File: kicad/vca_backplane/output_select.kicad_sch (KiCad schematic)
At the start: 54 parts, among them J12 AudioJack_729JH, J8 AudioJack_729JH, U1 DG442xY, U12 DG442xY, U13 NE5532, U3 MCP4822, U5 AS3360, U8 PCA9555PW, U9 DG442xY

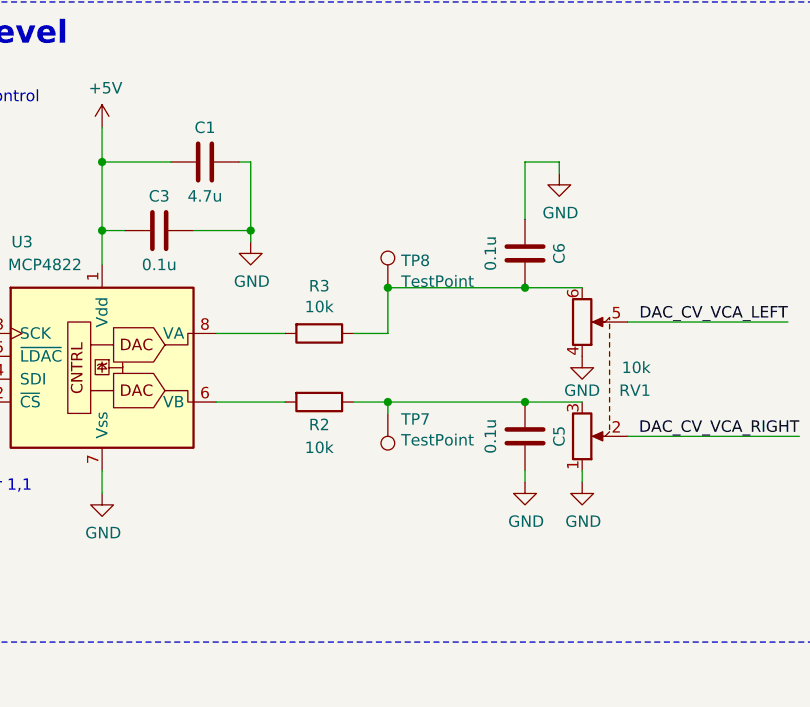
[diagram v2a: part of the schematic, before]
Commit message: power routing updated
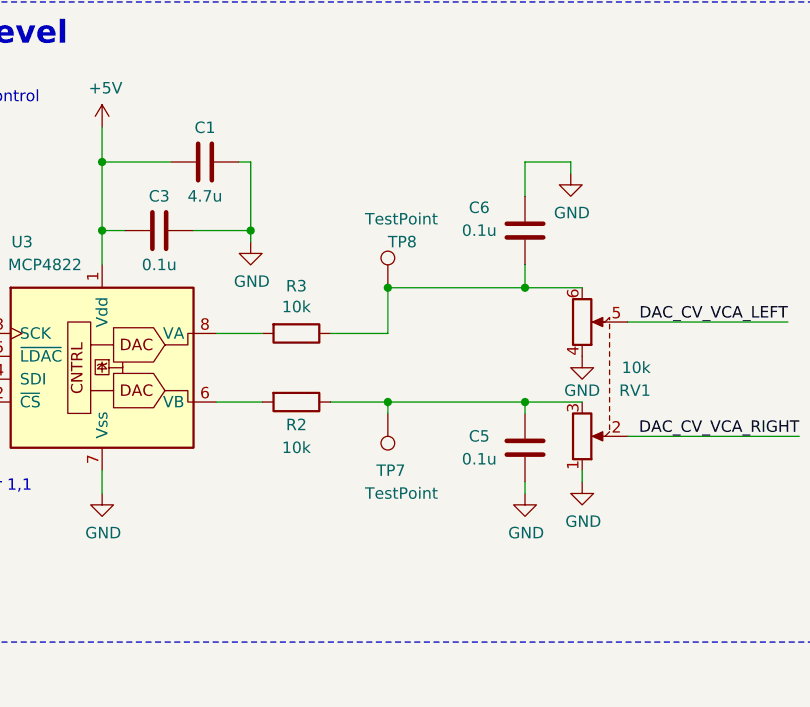
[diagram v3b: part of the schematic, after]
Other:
- moved on the sheet: C5, C6, R2, R3
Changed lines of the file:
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@@
     (stroke (width 0) (type default))
   )
-  (wire (pts (xy 86.36 151.13) (xy 90.17 151.13))
+  (wire (pts (xy 83.82 151.13) (xy 90.17 151.13))
     (stroke (width 0) (type default))
   )
@@
     (stroke (width 0) (type default))
   )
-  (wire (pts (xy 71.12 158.75) (xy 78.74 158.75))
+  (wire (pts (xy 71.12 158.75) (xy 76.2 158.75))
     (stroke (width 0) (type default))
   )
@@
     (stroke (width 0) (type default))
   )
+  (wire (pts (xy 105.41 168.91) (xy 105.41 167.64))
+    (stroke (width 0) (type default))
+  )
   (wire (pts (xy 318.77 71.12) (xy 316.23 71.12))
     (stroke (width 0) (type default))
@@
     (stroke (width 0) (type default))
   )
-  (wire (pts (xy 86.36 158.75) (xy 90.17 158.75))
+  (wire (pts (xy 83.82 158.75) (xy 90.17 158.75))
     (stroke (width 0) (type default))
   )
@@
     (stroke (width 0) (type default))
   )
-  (wire (pts (xy 71.12 151.13) (xy 78.74 151.13))
+  (wire (pts (xy 71.12 151.13) (xy 76.2 151.13))
     (stroke (width 0) (type default))
   )
@@
     (stroke (width 0) (type default))
   )
-  (wire (pts (xy 105.41 132.08) (xy 105.41 138.43))
+  (wire (pts (xy 105.41 132.08) (xy 105.41 135.89))
     (stroke (width 0) (type default))
   )
@@
     (stroke (width 0) (type default))
   )
-  (wire (pts (xy 109.22 133.35) (xy 109.22 132.08))
+  (wire (pts (xy 110.49 133.35) (xy 110.49 132.08))
     (stroke (width 0) (type default))
   )
@@
     (stroke (width 0) (type default))
   )
-  (wire (pts (xy 109.22 132.08) (xy 105.41 132.08))
+  (wire (pts (xy 110.49 132.08) (xy 105.41 132.08))
     (stroke (width 0) (type default))
   )
@@
     (stroke (width 0) (type default))
   )
-  (wire (pts (xy 105.41 166.37) (xy 105.41 167.64))
-    (stroke (width 0) (type default))
-  )
   (wire (pts (xy 269.24 144.78) (xy 270.51 144.78))
     (stroke (width 0) (type default))
@@
     (stroke (width 0) (type default))
   )
+  (wire (pts (xy 105.41 160.02) (xy 105.41 158.75))
+    (stroke (width 0) (type default))
+  )
   (wire (pts (xy 308.61 184.15) (xy 316.23 184.15))
     (stroke (width 0) (type default))
@@
     (stroke (width 0) (type default))
   )
+  (wire (pts (xy 105.41 143.51) (xy 105.41 146.05))
+    (stroke (width 0) (type default))
+  )
   (wire (pts (xy 336.55 24.13) (xy 316.23 24.13))
     (stroke (width 0) (type default))
@@
   (symbol (lib_id "Connector:TestPoint") (at 90.17 160.02 180) (unit 1)
     (in_bom yes) (on_board yes) (dnp no)
-    (property "Reference" "TP7" (at 91.6432 160.6804 0)
+    (property "Reference" "TP7" (at 88.9 166.37 0)
       (effects (font (size 1.27 1.27)) (justify right))
     )
-    (property "Value" "TestPoint" (at 91.6432 162.9918 0)
+    (property "Value" "TestPoint" (at 87.63 168.91 0)
       (effects (font (size 1.27 1.27)) (justify right))
     )
@@
   (symbol (lib_id "Connector:TestPoint") (at 90.17 146.05 0) (unit 1)
     (in_bom yes) (on_board yes) (dnp no)
-    (property "Reference" "TP8" (at 91.6432 143.0528 0)
+    (property "Reference" "TP8" (at 90.17 140.97 0)
       (effects (font (size 1.27 1.27)) (justify left))
     )
-    (property "Value" "TestPoint" (at 91.6432 145.3642 0)
+    (property "Value" "TestPoint" (at 87.63 138.43 0)
       (effects (font (size 1.27 1.27)) (justify left))
     )
@@
     )
   )
-  (symbol (lib_id "Device:R") (at 82.55 151.13 270) (unit 1)
+  (symbol (lib_id "Device:R") (at 80.01 151.13 270) (unit 1)
     (in_bom yes) (on_board yes) (dnp no)
-    (property "Reference" "R3" (at 82.55 145.8722 90)
+    (property "Reference" "R3" (at 80.01 145.8722 90)
       (effects (font (size 1.27 1.27)))
     )
-    (property "Value" "10k" (at 82.55 148.1836 90)
+    (property "Value" "10k" (at 80.01 148.1836 90)
       (effects (font (size 1.27 1.27)))
     )
-    (property "Footprint" "Resistor_SMD:R_0603_1608Metric" (at 82.55 149.352 90)
+    (property "Footprint" "Resistor_SMD:R_0603_1608Metric" (at 80.01 149.352 90)
       (effects (font (size 1.27 1.27)) hide)
     )
-    (property "Datasheet" "~" (at 82.55 151.13 0)
+    (property "Datasheet" "~" (at 80.01 151.13 0)
       (effects (font (size 1.27 1.27)) hide)
     )
-    (property "LCSC" "C25804" (at 82.55 151.13 0)
+    (property "LCSC" "C25804" (at 80.01 151.13 0)
       (effects (font (size 1.27 1.27)) hide)
     )
@@
     )
   )
-  (symbol (lib_id "Device:R") (at 82.55 158.75 270) (unit 1)
+  (symbol (lib_id "Device:R") (at 80.01 158.75 270) (unit 1)
     (in_bom yes) (on_board yes) (dnp no)
-    (property "Reference" "R2" (at 82.55 161.29 90)
+    (property "Reference" "R2" (at 80.01 161.29 90)
       (effects (font (size 1.27 1.27)))
     )
-    (property "Value" "10k" (at 82.55 163.83 90)
+    (property "Value" "10k" (at 80.01 163.83 90)
       (effects (font (size 1.27 1.27)))
     )
-    (property "Footprint" "Resistor_SMD:R_0603_1608Metric" (at 82.55 156.972 90)
+    (property "Footprint" "Resistor_SMD:R_0603_1608Metric" (at 80.01 156.972 90)
       (effects (font (size 1.27 1.27)) hide)
     )
-    (property "Datasheet" "~" (at 82.55 158.75 0)
+    (property "Datasheet" "~" (at 80.01 158.75 0)
       (effects (font (size 1.27 1.27)) hide)
     )
-    (property "LCSC" "C25804" (at 82.55 158.75 0)
+    (property "LCSC" "C25804" (at 80.01 158.75 0)
       (effects (font (size 1.27 1.27)) hide)
     )
@@
     )
   )
-  (symbol (lib_id "Device:C") (at 105.41 142.24 180) (unit 1)
+  (symbol (lib_id "Device:C") (at 105.41 139.7 180) (unit 1)
     (in_bom yes) (on_board yes) (dnp no)
-    (property "Reference" "C6" (at 109.22 142.24 90)
+    (property "Reference" "C6" (at 100.33 137.16 0)
       (effects (font (size 1.27 1.27)))
     )
-    (property "Value" "0.1u" (at 101.6 142.24 90)
+    (property "Value" "0.1u" (at 100.33 139.7 0)
       (effects (font (size 1.27 1.27)))
     )
-    (property "Footprint" "Capacitor_SMD:C_0603_1608Metric" (at 104.4448 138.43 0)
+    (property "Footprint" "Capacitor_SMD:C_0603_1608Metric" (at 104.4448 135.89 0)
       (effects (font (size 1.27 1.27)) hide)
     )
-    (property "Datasheet" "~" (at 105.41 142.24 0)
+    (property "Datasheet" "~" (at 105.41 139.7 0)
       (effects (font (size 1.27 1.27)) hide)
     )
-    (property "LCSC" "C14663" (at 105.41 142.24 0)
+    (property "LCSC" "C14663" (at 105.41 139.7 0)
       (effects (font (size 1.27 1.27)) hide)
     )
@@
     )
   )
-  (symbol (lib_id "Device:C") (at 105.41 162.56 180) (unit 1)
+  (symbol (lib_id "Device:C") (at 105.41 163.83 180) (unit 1)
     (in_bom yes) (on_board yes) (dnp no)
-    (property "Reference" "C5" (at 109.22 162.56 90)
+    (property "Reference" "C5" (at 100.33 162.56 0)
       (effects (font (size 1.27 1.27)))
     )
-    (property "Value" "0.1u" (at 101.6 162.56 90)
+    (property "Value" "0.1u" (at 100.33 165.1 0)
       (effects (font (size 1.27 1.27)))
     )
-    (property "Footprint" "Capacitor_SMD:C_0603_1608Metric" (at 104.4448 158.75 0)
+    (property "Footprint" "Capacitor_SMD:C_0603_1608Metric" (at 104.4448 160.02 0)
       (effects (font (size 1.27 1.27)) hide)
     )
-    (property "Datasheet" "~" (at 105.41 162.56 0)
+    (property "Datasheet" "~" (at 105.41 163.83 0)
       (effects (font (size 1.27 1.27)) hide)
     )
-    (property "LCSC" "C14663" (at 105.41 162.56 0)
+    (property "LCSC" "C14663" (at 105.41 163.83 0)
       (effects (font (size 1.27 1.27)) hide)
     )
@@
     )
   )
-  (symbol (lib_id "power:GND") (at 109.22 133.35 0) (unit 1)
+  (symbol (lib_id "power:GND") (at 110.49 133.35 0) (unit 1)
     (in_bom yes) (on_board yes) (dnp no)
-    (property "Reference" "#PWR028" (at 109.22 139.7 0)
+    (property "Reference" "#PWR028" (at 110.49 139.7 0)
       (effects (font (size 1.27 1.27)) hide)
     )
-    (property "Value" "GND" (at 109.347 137.7442 0)
+    (property "Value" "GND" (at 110.617 137.7442 0)
       (effects (font (size 1.27 1.27)))
     )
-    (property "Footprint" "" (at 109.22 133.35 0)
+    (property "Footprint" "" (at 110.49 133.35 0)
       (effects (font (size 1.27 1.27)) hide)
     )
-    (property "Datasheet" "" (at 109.22 133.35 0)
+    (property "Datasheet" "" (at 110.49 133.35 0)
       (effects (font (size 1.27 1.27)) hide)
     )
@@
     )
   )
-  (symbol (lib_id "power:GND") (at 105.41 167.64 0) (unit 1)
+  (symbol (lib_id "power:GND") (at 105.41 168.91 0) (unit 1)
     (in_bom yes) (on_board yes) (dnp no)
-    (property "Reference" "#PWR027" (at 105.41 173.99 0)
+    (property "Reference" "#PWR027" (at 105.41 175.26 0)
       (effects (font (size 1.27 1.27)) hide)
     )
-    (property "Value" "GND" (at 105.537 172.0342 0)
+    (property "Value" "GND" (at 105.537 173.3042 0)
       (effects (font (size 1.27 1.27)))
     )
-    (property "Footprint" "" (at 105.41 167.64 0)
+    (property "Footprint" "" (at 105.41 168.91 0)
       (effects (font (size 1.27 1.27)) hide)
     )
-    (property "Datasheet" "" (at 105.41 167.64 0)
+    (property "Datasheet" "" (at 105.41 168.91 0)
       (effects (font (size 1.27 1.27)) hide)
     )

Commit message: checkin before moving pi footprint a bit
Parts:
- removed R11, R20: 2k, Resistor_SMD:R_0603_1608Metric, symbol Device:R
- C12, C19: value 47u -> 22u
- R27, R28: footprint Resistor_SMD:R_1206_3216Metric -> Resistor_SMD:R_0603_1608Metric; LCSC (none) -> C22775
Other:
- moved on the sheet: C18
